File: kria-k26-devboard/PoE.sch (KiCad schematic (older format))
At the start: 24 parts, among them IC1 TPS2378DDA, Q1 PJA3441, U3 MAX5984AETI+T

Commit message: Finished reset logic, added crystal gen. to USB PHY, create power toggle for SD 3.0
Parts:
- renumbered C9 to C25, C10 to C26, C11 to C27, C12 to C28, C13 to C29, C14 to C30, C15 to C31, C16 to C32, C17 to C33, C18 to C34, Q1 to Q2, R1 to R12, R2 to R13, R3 to R14, R5 to R15, R4 to R16, U3 to U2
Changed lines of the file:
@@
 $Descr A4 11693 8268
 encoding utf-8
-Sheet 5 17
+Sheet 4 17
 Title ""
 Date "2022-03-10"
@@
 P 4000 1850
 AR Path="/63C44BC2/6253A5F4" Ref="R?"  Part="1"
-AR Path="/63C44BC2/62525BE1/6253A5F4" Ref="R2"  Part="1"
-F 0 "R2" V 3955 1920 60  0000 L CNN
+AR Path="/63C44BC2/62525BE1/6253A5F4" Ref="R13"  Part="1"
+F 0 "R13" V 3955 1920 60  0000 L CNN
 F 1 "R_24k9_0402" H 4000 1700 60  0001 C CNN
 F 2 "antmicro-footprints:0402-res" H 4200 2050 60  0001 L CNN
@@
 P 4000 2550
 AR Path="/63C44BC2/6253A5FD" Ref="R?"  Part="1"
-AR Path="/63C44BC2/62525BE1/6253A5FD" Ref="R3"  Part="1"
-F 0 "R3" V 3955 2620 60  0000 L CNN
+AR Path="/63C44BC2/62525BE1/6253A5FD" Ref="R14"  Part="1"
+F 0 "R14" V 3955 2620 60  0000 L CNN
 F 1 "R_63R4_0402" H 4000 2400 60  0001 C CNN
 F 2 "antmicro-footprints:0402-res" H 4200 2750 60  0001 L CNN
@@
 P 5550 3000
 AR Path="/63C44BC2/6253A612" Ref="#PWR?"  Part="1"
-AR Path="/63C44BC2/62525BE1/6253A612" Ref="#PWR0102"  Part="1"
-F 0 "#PWR0102" H 5550 2750 50  0001 C CNN
+AR Path="/63C44BC2/62525BE1/6253A612" Ref="#PWR019"  Part="1"
+F 0 "#PWR019" H 5550 2750 50  0001 C CNN
 F 1 "GNDD" H 5554 2845 50  0000 C CNN
 F 2 "" H 5550 3000 50  0001 C CNN
@@
 P 3750 2250
 AR Path="/63C44BC2/6253A644" Ref="C?"  Part="1"
-AR Path="/63C44BC2/62525BE1/6253A644" Ref="C10"  Part="1"
-F 0 "C10" V 3600 2200 60  0000 L CNN
+AR Path="/63C44BC2/62525BE1/6253A644" Ref="C26"  Part="1"
+F 0 "C26" V 3600 2200 60  0000 L CNN
 F 1 "C_100n_0805_100V" H 3750 2100 60  0001 C CNN
 F 2 "antmicro-footprints:0805-cap" H 3950 2450 60  0001 L CNN
@@
 P 6600 2200
 AR Path="/63C44BC2/6253A657" Ref="C?"  Part="1"
-AR Path="/63C44BC2/62525BE1/6253A657" Ref="C15"  Part="1"
-F 0 "C15" V 6450 2100 60  0000 L CNN
+AR Path="/63C44BC2/62525BE1/6253A657" Ref="C31"  Part="1"
+F 0 "C31" V 6450 2100 60  0000 L CNN
 F 1 "C_47u_ELEC_100V" H 6600 2050 60  0001 C CNN
 F 2 "antmicro-footprints:CP_Elec_10x10.5" H 6800 2400 60  0001 L CNN
@@
 P 5800 4550
 AR Path="/63C44BC2/6253A671" Ref="R?"  Part="1"
-AR Path="/63C44BC2/62525BE1/6253A671" Ref="R4"  Part="1"
-F 0 "R4" V 5755 4620 60  0000 L CNN
+AR Path="/63C44BC2/62525BE1/6253A671" Ref="R16"  Part="1"
+F 0 "R16" V 5755 4620 60  0000 L CNN
 F 1 "R_100k_0805" H 5800 4400 60  0001 C CNN
 F 2 "antmicro-footprints:0805-res" H 6000 4750 60  0001 L CNN
@@
 P 5250 6900
 AR Path="/63C44BC2/6253A6E5" Ref="C?"  Part="1"
-AR Path="/63C44BC2/62525BE1/6253A6E5" Ref="C13"  Part="1"
-F 0 "C13" V 5000 6800 60  0000 C CNN
+AR Path="/63C44BC2/62525BE1/6253A6E5" Ref="C29"  Part="1"
+F 0 "C29" V 5000 6800 60  0000 C CNN
 F 1 "C_1n0_0402" H 5250 6750 60  0001 C CNN
 F 2 "antmicro-footprints:0402-cap" H 5450 7100 60  0001 L CNN
@@
 P 2450 4800
 AR Path="/63C44BC2/6253A6EE" Ref="R?"  Part="1"
-AR Path="/63C44BC2/62525BE1/6253A6EE" Ref="R1"  Part="1"
-F 0 "R1" H 2400 4700 60  0000 L CNN
+AR Path="/63C44BC2/62525BE1/6253A6EE" Ref="R12"  Part="1"
+F 0 "R12" H 2400 4700 60  0000 L CNN
 F 1 "R_2M2_0805" H 2450 4650 60  0001 C CNN
 F 2 "antmicro-footprints:0805-res" H 2650 5000 60  0001 L CNN
@@
 P 2850 4800
 AR Path="/63C44BC2/6253A6F7" Ref="C?"  Part="1"
-AR Path="/63C44BC2/62525BE1/6253A6F7" Ref="C9"  Part="1"
-F 0 "C9" V 2700 4750 60  0000 L CNN
+AR Path="/63C44BC2/62525BE1/6253A6F7" Ref="C25"  Part="1"
+F 0 "C25" V 2700 4750 60  0000 L CNN
 F 1 "C_100n_0805_100V" H 2850 4650 60  0001 C CNN
 F 2 "antmicro-footprints:0805-cap" H 3050 5000 60  0001 L CNN
@@
 P 4100 4850
 AR Path="/63C44BC2/6253A708" Ref="C?"  Part="1"
-AR Path="/63C44BC2/62525BE1/6253A708" Ref="C11"  Part="1"
-F 0 "C11" V 3950 4800 60  0000 L CNN
+AR Path="/63C44BC2/62525BE1/6253A708" Ref="C27"  Part="1"
+F 0 "C27" V 3950 4800 60  0000 L CNN
 F 1 "C_100n_0805_100V" H 4100 4700 60  0001 C CNN
 F 2 "antmicro-footprints:0805-cap" H 4300 5050 60  0001 L CNN
@@
 P 4500 4800
 AR Path="/63C44BC2/6253A711" Ref="C?"  Part="1"
-AR Path="/63C44BC2/62525BE1/6253A711" Ref="C12"  Part="1"
-F 0 "C12" V 4350 4700 60  0000 L CNN
+AR Path="/63C44BC2/62525BE1/6253A711" Ref="C28"  Part="1"
+F 0 "C28" V 4350 4700 60  0000 L CNN
 F 1 "C_47u_ELEC_100V" H 4500 4650 60  0001 C CNN
 F 2 "antmicro-footprints:CP_Elec_10x10.5" H 4700 5000 60  0001 L CNN
@@
 P 5000 5600
 AR Path="/63C44BC2/6253A719" Ref="U?"  Part="1"
-AR Path="/63C44BC2/62525BE1/6253A719" Ref="U3"  Part="1"
-F 0 "U3" H 6125 5887 60  0000 C CNN
+AR Path="/63C44BC2/62525BE1/6253A719" Ref="U2"  Part="1"
+F 0 "U2" H 6125 5887 60  0000 C CNN
 F 1 "MAX5984AETI+T" H 6125 5781 60  0000 C CNN
 F 2 "antmicro-footprints:Maxim_MAX5984_TQFN-EP-28" H 6150 5840 60  0001 C CNN
@@
 P 5150 4400
 AR Path="/63C44BC2/6253A721" Ref="Q?"  Part="1"
-AR Path="/63C44BC2/62525BE1/6253A721" Ref="Q1"  Part="1"
-F 0 "Q1" V 5442 4650 50  0000 C CNN
+AR Path="/63C44BC2/62525BE1/6253A721" Ref="Q2"  Part="1"
+F 0 "Q2" V 5442 4650 50  0000 C CNN
 F 1 "PJA3441" V 5351 4650 50  0000 C CNN
 F 2 "antmicro-footprints:SOT-23-3" H 5150 4400 50  0001 C CNN
@@
 P 6200 2200
 AR Path="/63C44BC2/62542DEE" Ref="C?"  Part="1"
-AR Path="/63C44BC2/62525BE1/62542DEE" Ref="C14"  Part="1"
-F 0 "C14" V 6050 2100 60  0000 L CNN
+AR Path="/63C44BC2/62525BE1/62542DEE" Ref="C30"  Part="1"
+F 0 "C30" V 6050 2100 60  0000 L CNN
 F 1 "C_47u_ELEC_100V" H 6200 2050 60  0001 C CNN
 F 2 "antmicro-footprints:CP_Elec_10x10.5" H 6400 2400 60  0001 L CNN
@@
 	6200 2900 6600 2900
 $Comp
-L antmicroCapacitorsmisc:C_47u_16V_1206 C16
+L antmicroCapacitorsmisc:C_47u_16V_1206 C32
 U 1 1 6254E76E
 P 8850 2100
-F 0 "C16" H 8965 2145 60  0000 L CNN
+F 0 "C32" H 8965 2145 60  0000 L CNN
 F 1 "C_47u_16V_1206" H 8850 1950 60  0001 C CNN
 F 2 "antmicro-footprints:1206-cap" H 9050 2300 60  0001 L CNN
@@
 $EndComp
 $Comp
-L antmicroCapacitorsmisc:C_47u_16V_1206 C17
+L antmicroCapacitorsmisc:C_47u_16V_1206 C33
 U 1 1 6254ED87
 P 9400 2100
-F 0 "C17" H 9515 2145 60  0000 L CNN
+F 0 "C33" H 9515 2145 60  0000 L CNN
 F 1 "C_47u_16V_1206" H 9400 1950 60  0001 C CNN
 F 2 "antmicro-footprints:1206-cap" H 9600 2300 60  0001 L CNN
@@
 $EndComp
 $Comp
-L antmicroCapacitorsmisc:C_100n_0402_16V C18
+L antmicroCapacitorsmisc:C_100n_0402_16V C34
 U 1 1 6255055B
 P 10000 2100
-F 0 "C18" H 10115 2145 60  0000 L CNN
+F 0 "C34" H 10115 2145 60  0000 L CNN
 F 1 "C_100n_0402_16V" H 10000 1950 60  0001 C CNN
 F 2 "antmicro-footprints:0402-cap" H 10200 2300 60  0001 L CNN
@@
 Connection ~ 10000 1650
 $Comp
-L power:GND #PWR0103
+L power:GND #PWR020
 U 1 1 62590E73
 P 10000 2950
-F 0 "#PWR0103" H 10000 2700 50  0001 C CNN
+F 0 "#PWR020" H 10000 2700 50  0001 C CNN
 F 1 "GND" H 10005 2777 50  0000 C CNN
 F 2 "" H 10000 2950 50  0001 C CNN
@@
 	5450 6800 5450 6900
 $Comp
-L antmicroResistors0402:R_0R_0402 R5
+L antmicroResistors0402:R_0R_0402 R15
 U 1 1 62359494
 P 5200 6200
-F 0 "R5" H 5050 6250 60  0000 C CNN
+F 0 "R15" H 5050 6250 60  0000 C CNN
 F 1 "R_0R_0402" H 5200 6050 60  0001 C CNN
 F 2 "antmicro-footprints:0402-res" H 5400 6400 60  0001 L CNN

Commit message: Added second ETH interface, connect POE PSE
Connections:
- net labels added: POE_VC1, POE_VC2, POE_VC3, POE_VC4
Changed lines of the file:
@@
 POE_ACTIVE
 Wire Wire Line
-	2000 1450 1800 1450
-Wire Wire Line
-	2000 1850 1800 1850
-Wire Wire Line
-	2000 2450 1800 2450
-Wire Wire Line
-	2000 2850 1800 2850
+	2000 1450 1500 1450
+Wire Wire Line
+	2000 1850 1500 1850
+Wire Wire Line
+	2000 2450 1500 2450
+Wire Wire Line
+	2000 2850 1500 2850
 Connection ~ 3750 1650
 Wire Wire Line
@@
 	0    -1   1    0
 $EndComp
-Text Label 2050 5150 2    50   ~ 0
-VSS_POE_OUT
-Text Label 2050 4350 2    50   ~ 0
-VDD_POE_OUT
 Wire Wire Line
 	6000 4350 5800 4350
@@
 	2500 7000 2600 7000
 Connection ~ 2600 7000
-Text HLabel 1650 1300 0    50   Input ~ 0
+Text HLabel 1350 1300 0    50   Input ~ 0
 POE_VC[1..4]
 Wire Bus Line
-	1650 1300 1700 1300
+	1350 1300 1400 1300
 Entry Wire Line
-	1800 1450 1700 1350
+	1500 1450 1400 1350
 Entry Wire Line
-	1800 1850 1700 1750
+	1500 1850 1400 1750
 Entry Wire Line
-	1800 2450 1700 2350
+	1500 2450 1400 2350
 Entry Wire Line
-	1800 2850 1700 2750
+	1500 2850 1400 2750
+Text Label 1500 1450 0    50   ~ 0
+POE_VC1
+Text Label 1500 1850 0    50   ~ 0
+POE_VC2
+Text Label 1500 2450 0    50   ~ 0
+POE_VC3
+Text Label 1500 2850 0    50   ~ 0
+POE_VC4
 Wire Bus Line
-	1700 1300 1700 2750
+	1400 1300 1400 2750
+Text HLabel 2050 4350 0    50   Input ~ 0
+VDD_POE_OUT
+Text HLabel 2050 5150 0    50   Input ~ 0
+VSS_POE_OUT
 $EndSCHEMATC

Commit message: Removed PoE PSE and second ETH interface
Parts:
- removed C25, C27: C_100n_0805_100V, antmicro-footprints:0805-cap, symbol antmicroCapacitorsmisc:C_100n_0805_100V
- removed C28: C_47u_ELEC_100V, antmicro-footprints:CP_Elec_10x10.5, symbol antmicroCapacitorspol:C_47u_ELEC_100V
- removed C29: C_1n0_0402, antmicro-footprints:0402-cap, symbol antmicroCapacitors0402:C_1n0_0402
- removed D3: 1N4448WS, Diode_SMD:D_SOD-323, symbol Diode:1N4448WS
- removed D5: SMAJ58A-13-F, antmicro-footprints:DO-214AC, symbol antmicroDiodesRectifiersSingle:SMAJ58A-13-F
- removed Q2: PJA3441, antmicro-footprints:SOT-23-3, symbol antmicroTransistorsFETsMOSFETsSingle:PJA3441
- removed R12: R_2M2_0805, antmicro-footprints:0805-res, symbol antmicroResistorsmisc:R_2M2_0805
- removed R15: R_0R_0402, antmicro-footprints:0402-res, symbol antmicroResistors0402:R_0R_0402
- removed R16: R_100k_0805, antmicro-footprints:0805-res, symbol antmicroResistorsmisc:R_100k_0805
- removed U2: MAX5984AETI+T, antmicro-footprints:Maxim_MAX5984_TQFN-EP-28, symbol antmicroPMICPowerDistributionSwitchesLoadDrivers:MAX5984AETI+T
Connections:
- net labels removed: VDD_POE_OUT, VSS_POE_OUT
- wire segments 153 -> 75
- no-connect marks 3 -> 1
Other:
- note removed: "DNM - Activate midspan collision avoidance"
- note removed: "PoE PSE\n\n"
- moved on the sheet: C26, C30, C31, C32, C33, C34, D1, D2, D4, IC1, PS1, R13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

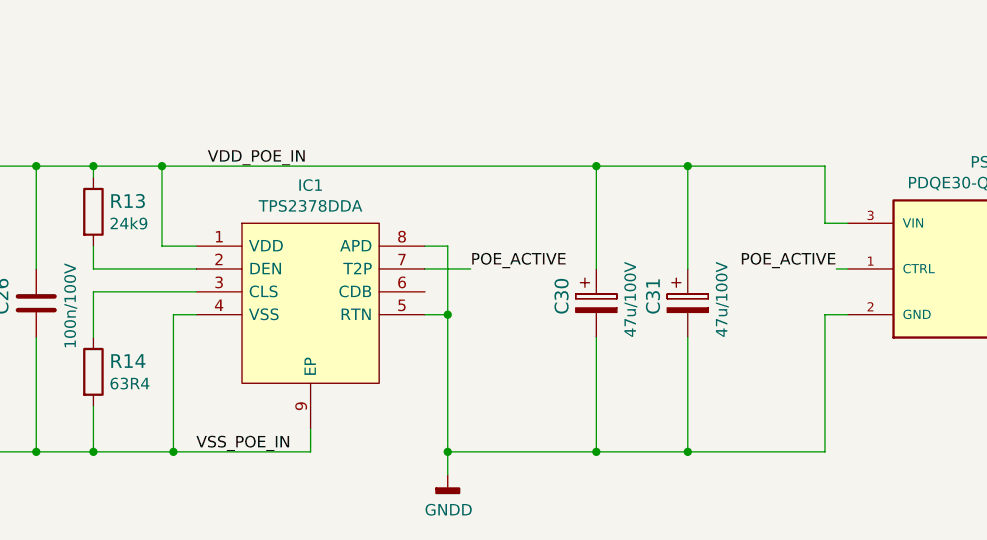
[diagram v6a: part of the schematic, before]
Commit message: Initial placement of power supply
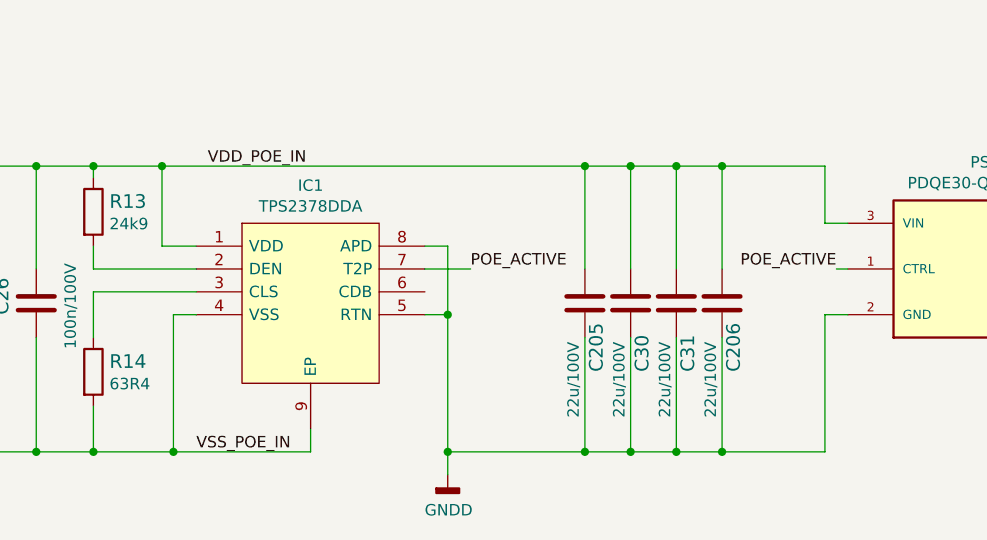
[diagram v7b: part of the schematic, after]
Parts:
- removed C30, C31: C_47u_ELEC_100V, antmicro-footprints:CP_Elec_10x10.5, symbol antmicroCapacitorspol:C_47u_ELEC_100V
- added C205, C206, C30, C31: C_22u_2220_100V, antmicro-footprints:2220-cap, symbol antmicroCapacitorsmisc:C_22u_2220_100V
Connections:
- net GNDD: now also C205.2, C206.2, C30.2, C31.2
- net VDD_POE_IN: now also C205.1, C206.1, C30.1, C31.1
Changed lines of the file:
@@
 	7400 3700 7500 3700
 Wire Wire Line
-	4500 3450 6400 3450
+	4500 3450 6350 3450
 Wire Wire Line
 	5750 4100 5750 4700
 Wire Wire Line
-	5750 4700 6400 4700
+	5750 4700 6350 4700
 Wire Wire Line
 	7400 4700 7400 4100
@@
 Wire Wire Line
 	5850 3900 5650 3900
-$Comp
-L antmicroCapacitorspol:C_47u_ELEC_100V C?
-U 1 1 6253A657
-P 6800 4000
-AR Path="/63C44BC2/6253A657" Ref="C?"  Part="1"
-AR Path="/63C44BC2/62525BE1/6253A657" Ref="C31"  Part="1"
-F 0 "C31" V 6650 3900 60  0000 L CNN
-F 1 "C_47u_ELEC_100V" H 6800 3850 60  0001 C CNN
-F 2 "antmicro-footprints:CP_Elec_10x10.5" H 7000 4200 60  0001 L CNN
-F 3 "https://industrial.panasonic.com/cdbs/www-data/pdf/RDE0000/ABA0000C1151.pdf" H 6800 4000 50  0001 C CNN
-F 4 "PANASONIC" H 7000 4400 60  0001 L CNN "Manufacturer"
-F 5 "EEEHA2A470UP" H 7000 4300 60  0001 L CNN "MPN"
-F 6 "47u/100V" V 6950 3800 50  0000 L CNN "Val"
-	1    6800 4000
-	1    0    0    -1
-$EndComp
-Wire Wire Line
-	6800 3900 6800 3450
-Connection ~ 6800 3450
-Wire Wire Line
-	6800 3450 7400 3450
-Wire Wire Line
-	6800 4200 6800 4700
-Connection ~ 6800 4700
-Wire Wire Line
-	6800 4700 7400 4700
+Wire Wire Line
+	6750 3900 6750 3450
+Wire Wire Line
+	6750 4200 6750 4700
 Text Label 7450 3900 2    50   ~ 0
 POE_ACTIVE
 Wire Wire Line
 	7450 3900 7500 3900
-$Comp
-L antmicroCapacitorspol:C_47u_ELEC_100V C?
-U 1 1 62542DEE
-P 6400 4000
-AR Path="/63C44BC2/62542DEE" Ref="C?"  Part="1"
-AR Path="/63C44BC2/62525BE1/62542DEE" Ref="C30"  Part="1"
-F 0 "C30" V 6250 3900 60  0000 L CNN
-F 1 "C_47u_ELEC_100V" H 6400 3850 60  0001 C CNN
-F 2 "antmicro-footprints:CP_Elec_10x10.5" H 6600 4200 60  0001 L CNN
-F 3 "https://industrial.panasonic.com/cdbs/www-data/pdf/RDE0000/ABA0000C1151.pdf" H 6400 4000 50  0001 C CNN
-F 4 "PANASONIC" H 6600 4400 60  0001 L CNN "Manufacturer"
-F 5 "EEEHA2A470UP" H 6600 4300 60  0001 L CNN "MPN"
-F 6 "47u/100V" V 6550 3800 50  0000 L CNN "Val"
-	1    6400 4000
-	1    0    0    -1
-$EndComp
-Wire Wire Line
-	6400 3900 6400 3450
-Wire Wire Line
-	6400 4200 6400 4700
-Connection ~ 6400 3450
-Wire Wire Line
-	6400 3450 6800 3450
-Connection ~ 6400 4700
-Wire Wire Line
-	6400 4700 6800 4700
+Wire Wire Line
+	6350 3900 6350 3450
+Wire Wire Line
+	6350 4200 6350 4700
 $Comp
 L antmicroCapacitorsmisc:C_47u_16V_1206 C32
@@
 Text Label 1700 4650 0    50   ~ 0
 POE_VC4
+$Comp
+L antmicroCapacitorsmisc:C_22u_2220_100V C205
+U 1 1 6A074DA7
+P 6350 4050
+F 0 "C205" V 6400 3750 60  0000 L CNN
+F 1 "C_22u_2220_100V" H 6350 3900 60  0001 C CNN
+F 2 "antmicro-footprints:2220-cap" H 6550 4250 60  0001 L CNN
+F 3 "" H 6350 4050 50  0001 C CNN
+F 4 "TDK" H 6550 4450 60  0001 L CNN "Manufacturer"
+F 5 "C5750X7S2A226M280KB" H 6550 4350 60  0001 L CNN "MPN"
+F 6 "22u/100V" V 6300 3550 50  0000 L CNN "Val"
+	1    6350 4050
+	1    0    0    -1
+$EndComp
+$Comp
+L antmicroCapacitorsmisc:C_22u_2220_100V C30
+U 1 1 6A0791F7
+P 6550 4050
+F 0 "C30" V 6600 3750 60  0000 L CNN
+F 1 "C_22u_2220_100V" H 6550 3900 60  0001 C CNN
+F 2 "antmicro-footprints:2220-cap" H 6750 4250 60  0001 L CNN
+F 3 "" H 6550 4050 50  0001 C CNN
+F 4 "TDK" H 6750 4450 60  0001 L CNN "Manufacturer"
+F 5 "C5750X7S2A226M280KB" H 6750 4350 60  0001 L CNN "MPN"
+F 6 "22u/100V" V 6500 3550 50  0000 L CNN "Val"
+	1    6550 4050
+	1    0    0    -1
+$EndComp
+$Comp
+L antmicroCapacitorsmisc:C_22u_2220_100V C31
+U 1 1 6A0794FE
+P 6750 4050
+F 0 "C31" V 6800 3750 60  0000 L CNN
+F 1 "C_22u_2220_100V" H 6750 3900 60  0001 C CNN
+F 2 "antmicro-footprints:2220-cap" H 6950 4250 60  0001 L CNN
+F 3 "" H 6750 4050 50  0001 C CNN
+F 4 "TDK" H 6950 4450 60  0001 L CNN "Manufacturer"
+F 5 "C5750X7S2A226M280KB" H 6950 4350 60  0001 L CNN "MPN"
+F 6 "22u/100V" V 6700 3550 50  0000 L CNN "Val"
+	1    6750 4050
+	1    0    0    -1
+$EndComp
+$Comp
+L antmicroCapacitorsmisc:C_22u_2220_100V C206
+U 1 1 6A079825
+P 6950 4050
+F 0 "C206" V 7000 3750 60  0000 L CNN
+F 1 "C_22u_2220_100V" H 6950 3900 60  0001 C CNN
+F 2 "antmicro-footprints:2220-cap" H 7150 4250 60  0001 L CNN
+F 3 "" H 6950 4050 50  0001 C CNN
+F 4 "TDK" H 7150 4450 60  0001 L CNN "Manufacturer"
+F 5 "C5750X7S2A226M280KB" H 7150 4350 60  0001 L CNN "MPN"
+F 6 "22u/100V" V 6900 3550 50  0000 L CNN "Val"
+	1    6950 4050
+	1    0    0    -1
+$EndComp
+Connection ~ 6350 3450
+Connection ~ 6750 3450
+Wire Wire Line
+	6350 3450 6550 3450
+Connection ~ 6350 4700
+Connection ~ 6750 4700
+Wire Wire Line
+	6750 4700 6950 4700
+Wire Wire Line
+	6350 4700 6550 4700
+Wire Wire Line
+	6550 4200 6550 4700
+Connection ~ 6550 4700
+Wire Wire Line
+	6550 4700 6750 4700
+Wire Wire Line
+	6950 4200 6950 4700
+Connection ~ 6950 4700
+Wire Wire Line
+	6950 4700 7400 4700
+Wire Wire Line
+	6950 3900 6950 3450
+Wire Wire Line
+	6750 3450 6950 3450
+Connection ~ 6950 3450
+Wire Wire Line
+	6950 3450 7400 3450
+Wire Wire Line
+	6550 3900 6550 3450
 Wire Bus Line
 	1600 3100 1600 4550
+Connection ~ 6550 3450
+Wire Wire Line
+	6550 3450 6750 3450
 $EndSCHEMATC
